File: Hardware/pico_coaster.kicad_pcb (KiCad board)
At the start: 2 copper layers, 90 x 90 mm, 140 parts, among them J4 Conn_01x04, SW1 SW_Push, SW2 SW_Push, SW3 SW_Push, SW4 SW_Push, SW5 SW_Push, SW6 SW_Push, U1 NCP1117-3.3_SOT223, U2 W25Q128JVS, U3 RP2040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

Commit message: prior layout changes
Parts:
- Y1: moved to F.Cu
- moved U1 12.9 mm to (230.1, 60.1)

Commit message: add USB-c connector on top layer
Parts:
- added J3: Conn_02x06_Odd_Even, Connector_PinHeader_2.54mm:PinHeader_2x06_P2.54mm_Vertical, F.Cu at (178.4, 86.3)
- added J5: USB_C_Receptacle_USB2.0, Connector_USB:USB_C_Receptacle_Amphenol_12401610E4-2A_CircularHoles, F.Cu at (203.4, 39.2)
- R2, R3: moved to F.Cu
- moved SW1 85.2 mm to (144.5, 24.6)
- moved SW6 60.8 mm to (131.3, 24.8)
- moved R2 9.31 mm to (201.5, 51.9)
- moved J4 8.42 mm to (243.4, 83.6)
- moved R3 5.91 mm to (203.2, 51.9)
- moved U2 4.41 mm to (186.3, 59.4)
- moved D3 2.10 mm to (195.0, 39.7), turned to 90 degrees
- moved D4 1.80 mm to (211.9, 39.8), turned to 90 degrees
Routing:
- net +3V3: track 372.0 -> 326.2 mm
- net GND: track 238.8 -> 218.9 mm
- net Net-(D10-Pad2): track 19.3 -> 4.53 mm
- net VBUS: track 1.80 -> 9.21 mm
- net Net-(D2-Pad2): track 19.9 -> 14.2 mm
- net Net-(D4-Pad2): track 19.4 -> 13.8 mm
- net Net-(R3-Pad2): track 0.00 -> 4.48 mm
- net Net-(R2-Pad2): track 0.00 -> 4.42 mm
- net USB_DP: track 8.19 -> 12.6 mm, vias 0 -> 2
- net Net-(D3-Pad2): track 19.7 -> 17.8 mm
- net USB_DM: track 14.7 -> 14.4 mm, vias 3 -> 2

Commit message: route the Resistors for the USB Connector
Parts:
- moved R4 86.9 mm to (207.9, 47.0), turned to 180 degrees
- moved R5 83.5 mm to (199.1, 47.0), turned to 180 degrees
- turned U1 to 180 degrees
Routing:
- net VBUS: track 9.21 -> 49.5 mm, vias 0 -> 2
- net GND: track 218.9 -> 241.9 mm
- net +3V3: track 326.2 -> 339.5 mm, vias 0 -> 2
- net Net-(J5-PadB5): track 0.00 -> 9.12 mm, vias 0 -> 2
- net Net-(J5-PadA5): track 0.00 -> 4.71 mm

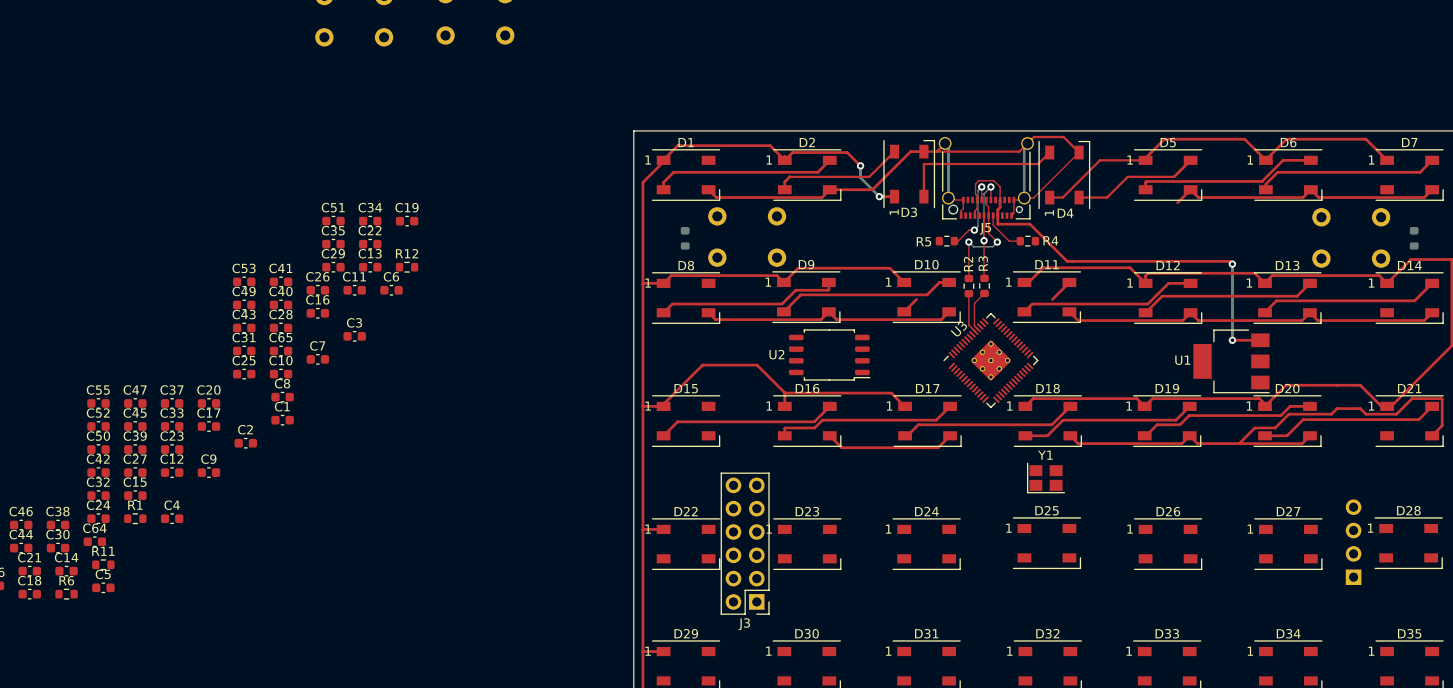
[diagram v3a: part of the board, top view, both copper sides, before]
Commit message: Routing RP2040 Caps, Memory and PMod Connector
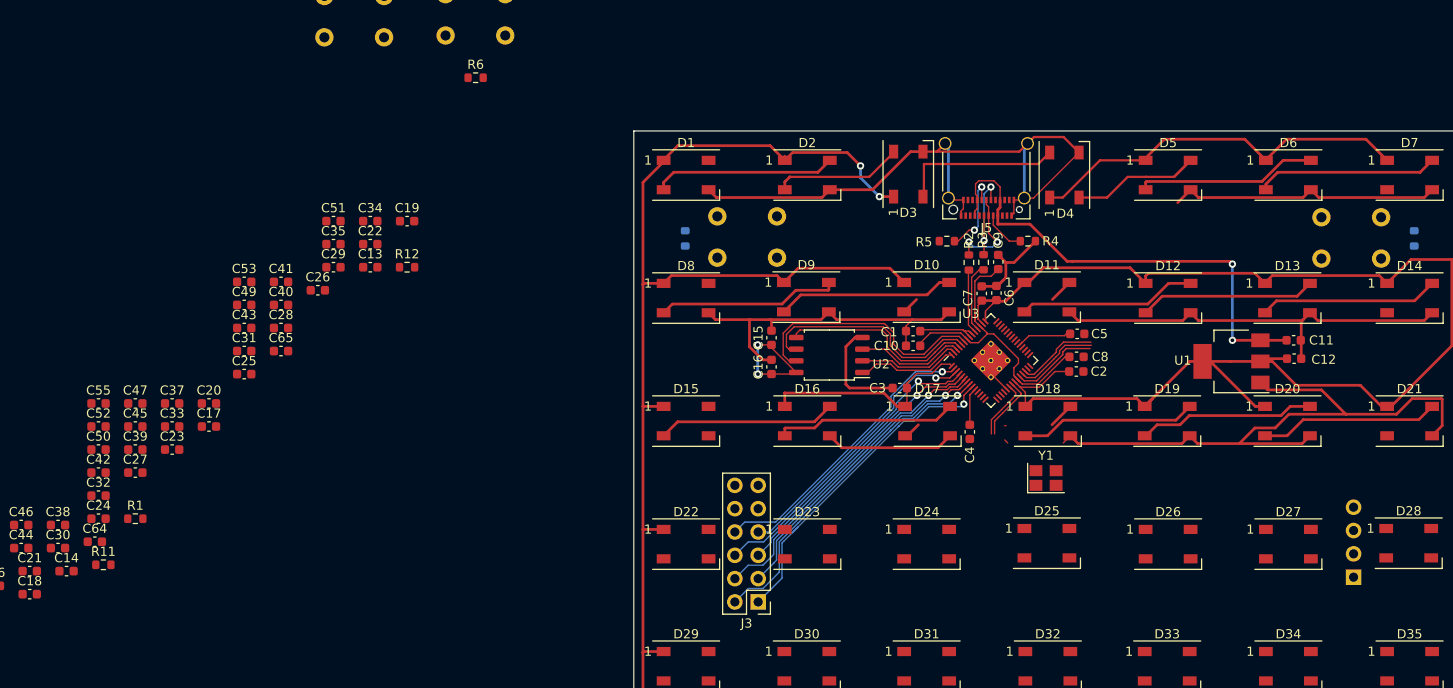
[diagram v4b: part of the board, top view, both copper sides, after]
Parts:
- moved C12 122.8 mm to (236.9, 59.8)
- moved C5 109.6 mm to (213.3, 57.1)
- moved C11 102.4 mm to (236.9, 57.8)
- moved C2 90.8 mm to (213.2, 61.2)
- moved C9 89.0 mm to (204.7, 49.3), turned to 90 degrees
- moved C4 87.4 mm to (201.6, 67.8), turned to 270 degrees
- moved C8 86.6 mm to (213.2, 59.6)
- moved C7 72.7 mm to (202.9, 52.7), turned to 90 degrees
- moved R6 71.8 mm to (147.8, 29.2)
- moved C15 71.4 mm to (180.0, 57.5), turned to 90 degrees
- moved C1 69.4 mm to (195.4, 56.8), turned to 180 degrees
- moved C10 68.9 mm to (195.4, 58.4), turned to 180 degrees
- moved C6 65.9 mm to (204.5, 52.6), turned to 90 degrees
- moved C3 59.6 mm to (194.0, 63.0), turned to 180 degrees
- moved C16 49.8 mm to (180.0, 60.7), turned to 90 degrees
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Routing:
- net +3V3: track 339.5 -> 398.7 mm, vias 2 -> 4
- net GND: track 241.9 -> 295.2 mm
- net GPIO_6: track 0.00 -> 37.5 mm, vias 0 -> 1
- net GPIO_7: track 0.00 -> 36.8 mm, vias 0 -> 1
- net GPIO_4: track 0.00 -> 35.7 mm, vias 0 -> 1
- net +1V1: track 0.04 -> 34.0 mm
- net GPIO_2: track 0.00 -> 33.5 mm, vias 0 -> 1
- net GPIO_5: track 0.00 -> 32.9 mm, vias 0 -> 1
- net GPIO_0: track 0.00 -> 32.0 mm, vias 0 -> 1
- net GPIO_3: track 0.00 -> 30.6 mm, vias 0 -> 1
- net GPIO_1: track 0.00 -> 30.1 mm, vias 0 -> 1
- net QSPI_SD3: track 0.00 -> 27.5 mm
- net QSPI_SCLK: track 0.00 -> 25.2 mm
- net QSPI_SD0: track 0.00 -> 21.6 mm
- net Net-(D17-Pad2): track 19.3 -> 4.78 mm
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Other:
- net class Default: clearance 0.2 -> 0.15
- rule pad_to_mask_clearance: 0 -> 0.02
- rule trace_clearance: 0.2 -> 0.15
- rule trace_min: 0.127 -> 0.1

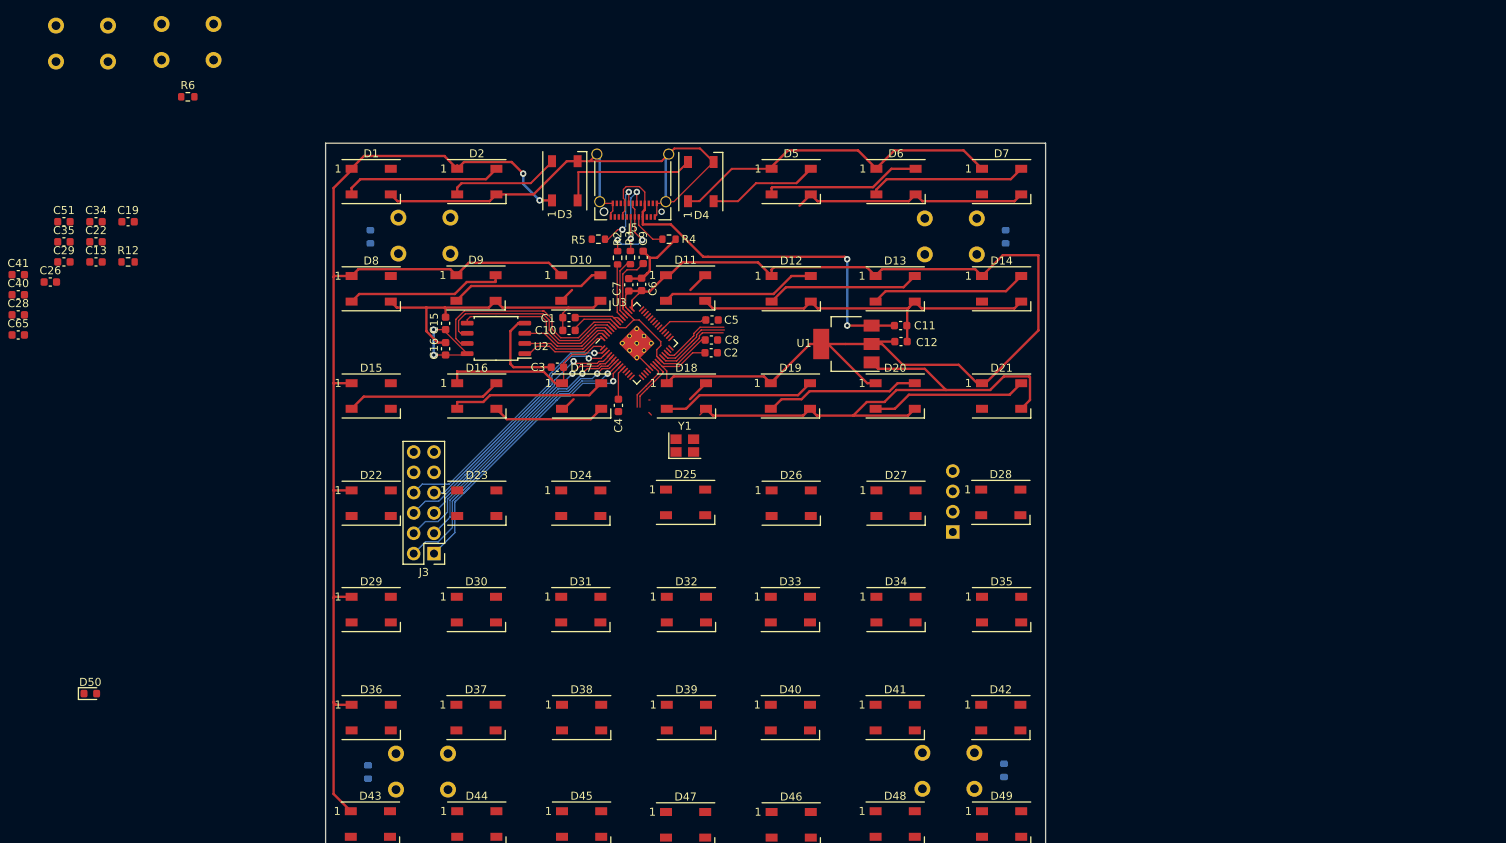
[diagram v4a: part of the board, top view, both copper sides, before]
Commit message: Route the GPIO buttons
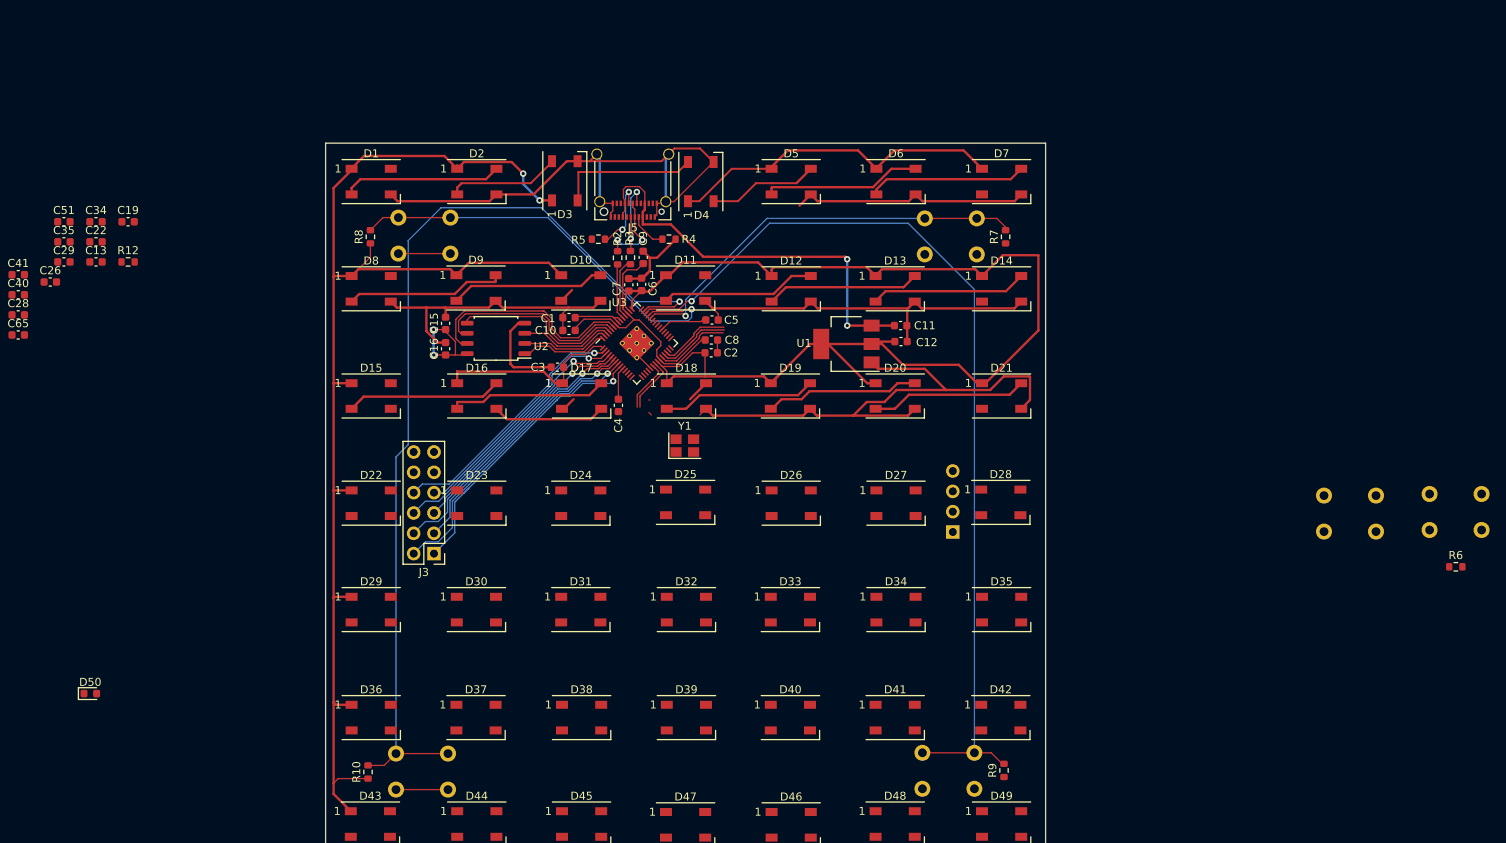
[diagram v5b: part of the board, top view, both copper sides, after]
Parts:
- R10, R7, R8, R9: moved to F.Cu
- moved SW1 169.0 mm to (303.0, 83.3)
- moved SW6 169.0 mm to (289.8, 83.5)
- moved R6 169.0 mm to (306.3, 88.0)
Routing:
- net GPIO29: track 0.00 -> 120.8 mm, vias 0 -> 1
- net GPIO28: track 0.00 -> 117.9 mm, vias 0 -> 1
- net GPIO27: track 0.00 -> 53.1 mm, vias 0 -> 1
- net GPIO26: track 0.00 -> 51.8 mm, vias 0 -> 1
- net GND: track 295.2 -> 311.5 mm
- net +3V3: track 398.7 -> 409.9 mm
- net Net-(D10-Pad2): track 4.53 -> 1.91 mm

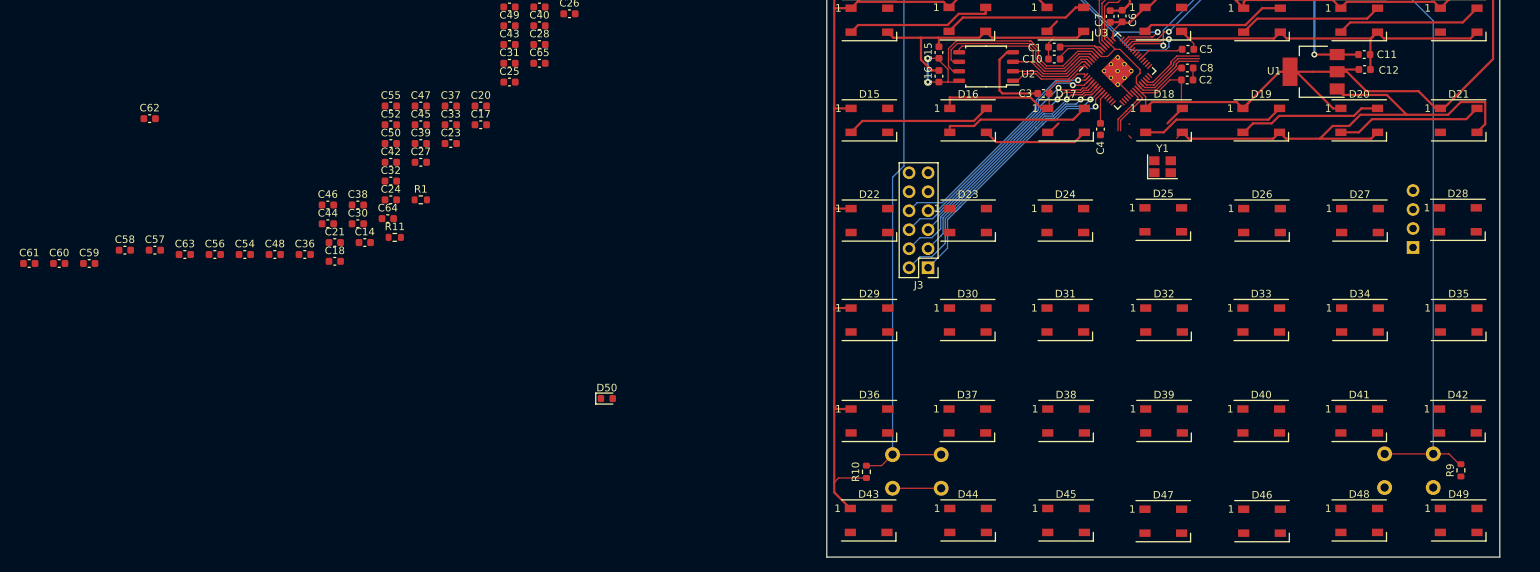
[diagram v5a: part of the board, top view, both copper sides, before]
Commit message: Routing Bottom row of RGB LEDs
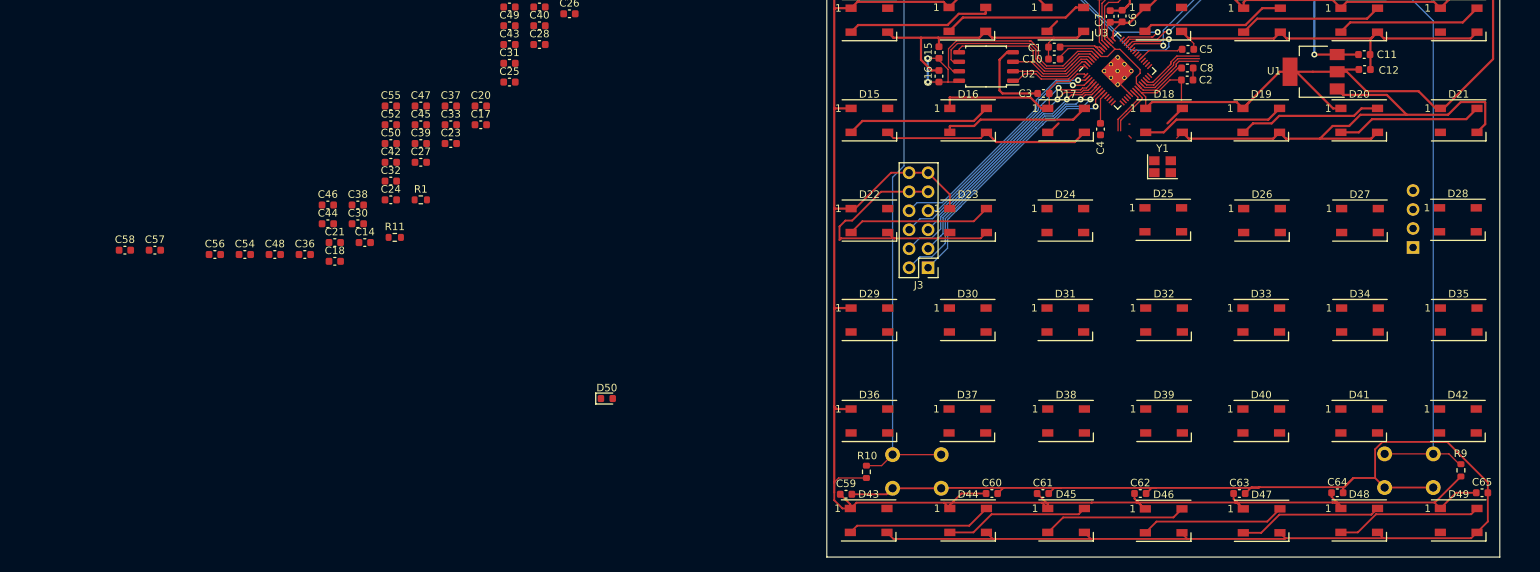
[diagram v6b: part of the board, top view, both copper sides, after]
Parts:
- moved C63 144.6 mm to (220.2, 116.5)
- moved C62 141.6 mm to (206.9, 116.5)
- moved C61 139.0 mm to (193.9, 116.5)
- moved C65 138.5 mm to (252.6, 116.4)
- moved C64 132.2 mm to (233.3, 116.4)
- moved C60 128.5 mm to (187.1, 116.5)
- moved C59 105.8 mm to (167.6, 116.6)
- moved D47 13.2 mm to (223.2, 120.2)
- moved D46 13.2 mm to (210.1, 120.2)
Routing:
- net GND: track 311.5 -> 559.2 mm
- net +3V3: track 409.9 -> 544.6 mm
- net Net-(D48-Pad2): track 0.00 -> 19.5 mm
- net Net-(D43-Pad2): track 0.00 -> 19.5 mm
- net Net-(D22-Pad2): track 0.00 -> 19.4 mm
- net Net-(D46-Pad2): track 0.00 -> 19.3 mm
- net Net-(D44-Pad2): track 0.00 -> 19.3 mm
- net Net-(D47-Pad2): track 0.00 -> 19.3 mm
- net Net-(D45-Pad2): track 0.00 -> 19.3 mm
